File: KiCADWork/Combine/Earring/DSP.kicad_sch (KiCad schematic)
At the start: 39 parts, among them J1 Screw_Terminal_01x01, J2 Screw_Terminal_01x02, SW2 SW_DIP_x01, U3 NRF52833-QDAA-R7, Y1 XL7EL89CKI-111YLC-32M, Y2 X161032768KLD2SI

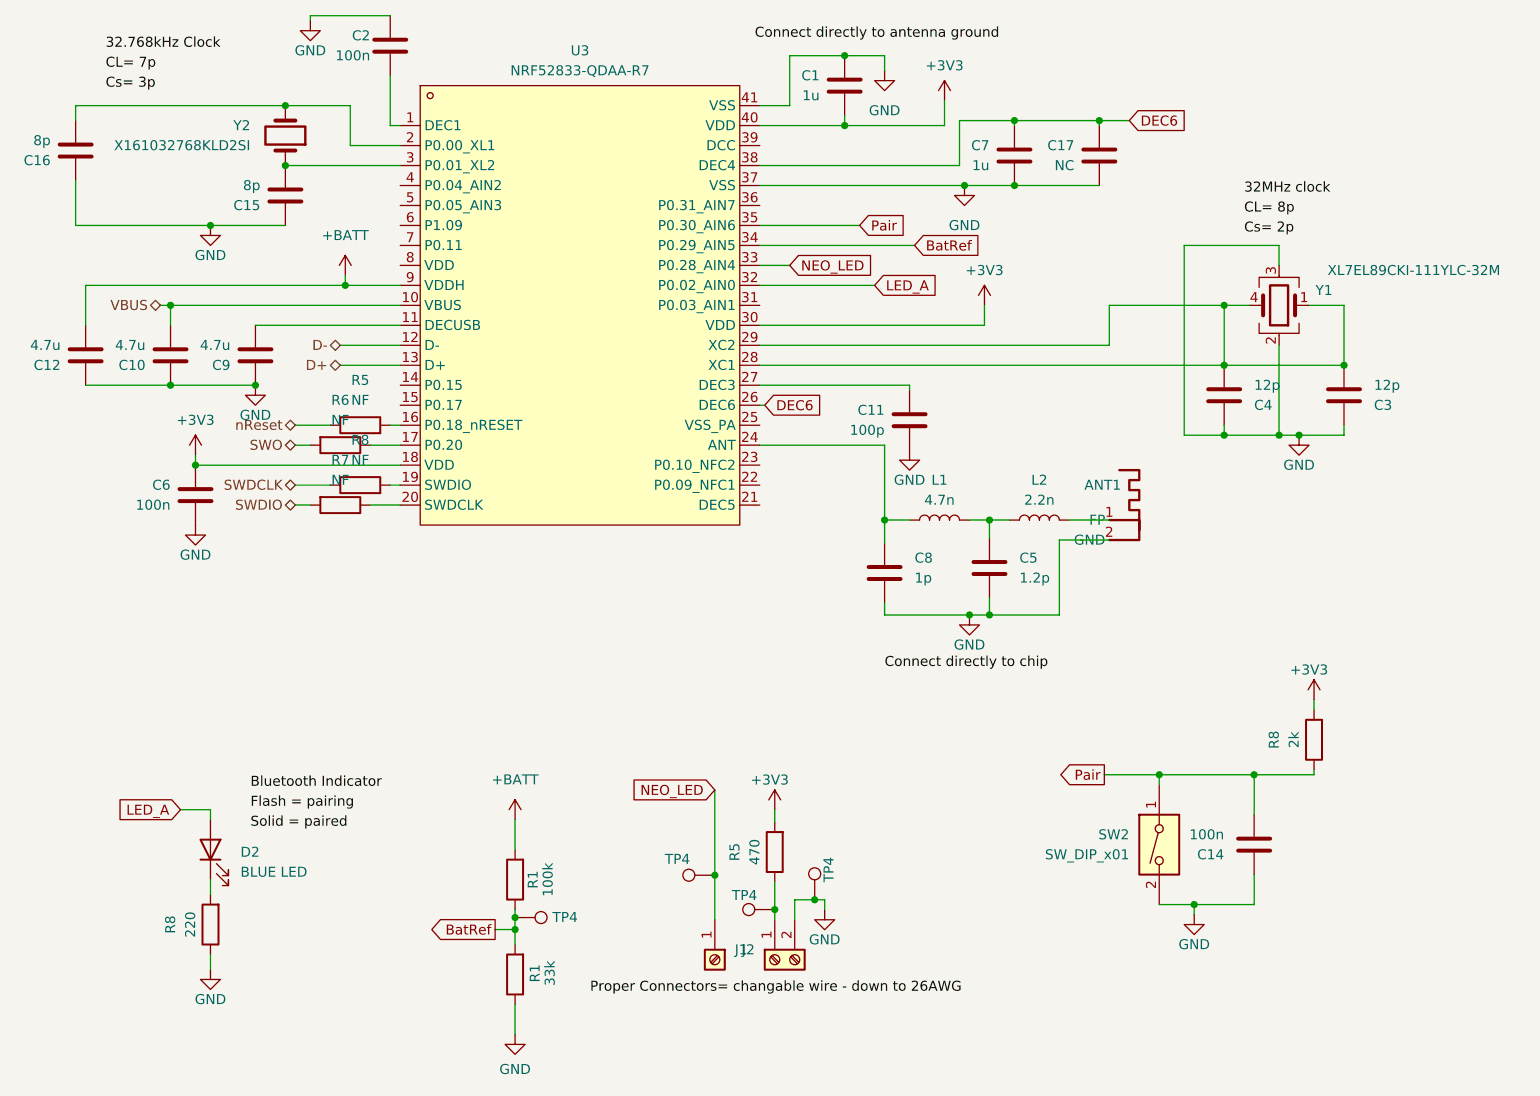
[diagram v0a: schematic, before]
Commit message: Completing the combined layout
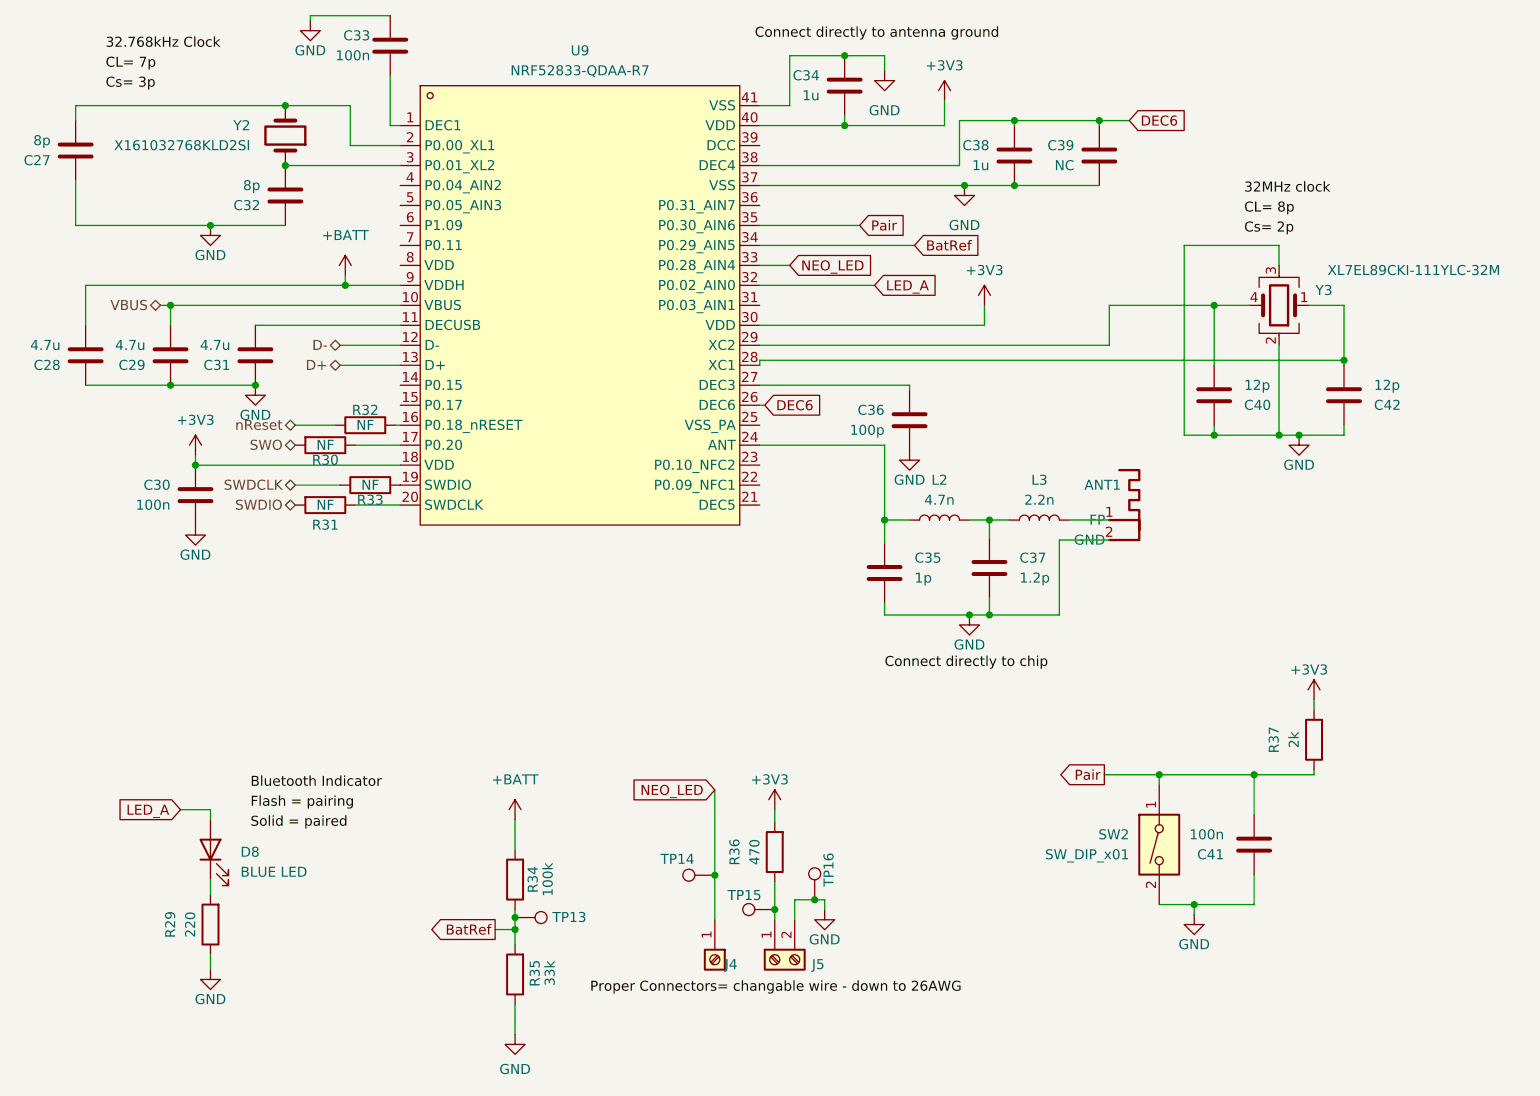
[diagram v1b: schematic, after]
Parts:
- renumbered C16 to C27, C12 to C28, C10 to C29, C6 to C30, C9 to C31, C15 to C32, C2 to C33, C1 to C34, C8 to C35, C11 to C36, C5 to C37, C7 to C38, C17 to C39, C4 to C40, C14 to C41, C3 to C42, D2 to D8, J1 to J4, J2 to J5, L1 to L2, L2 to L3, R8 to R29, R6 to R30, R7 to R31, R5 to R32, R8 to R33, R1 to R34, R1 to R35, R5 to R36, R8 to R37, TP4 to TP13, TP4 to TP14, TP4 to TP15, TP4 to TP16, U3 to U9, Y1 to Y3
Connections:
- net at C40.2, U9.29 (XC2), Y3.4: no longer C42.2, U9.28 (XC1), Y3.1
- new net: C42.2, U9.28 (XC1), Y3.1
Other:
- moved on the sheet: C40, R30, R31, R32, R33
